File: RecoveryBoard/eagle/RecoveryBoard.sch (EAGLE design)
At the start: 96 parts, among them Q1 BSS123, Q2 BSS123, Q3 BSS123, Q4 BPR-301, Q5 BPR-301, Q6 MOSFET-PCH-SOT23-6, U1 STM32F042K6, U10 TPS63070, U2 BD62120AEFJ-E2, U3 H11F1SR2M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

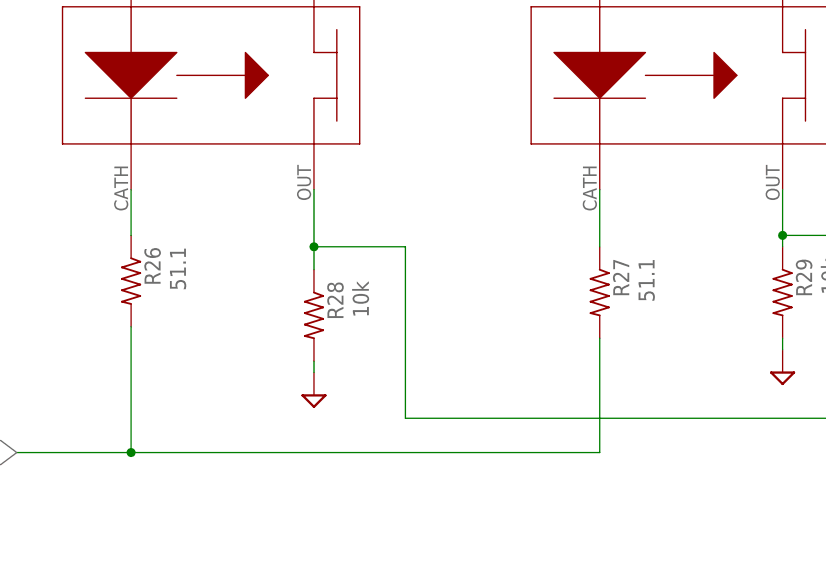
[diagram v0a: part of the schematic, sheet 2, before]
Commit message: added camera board folder and git ignore
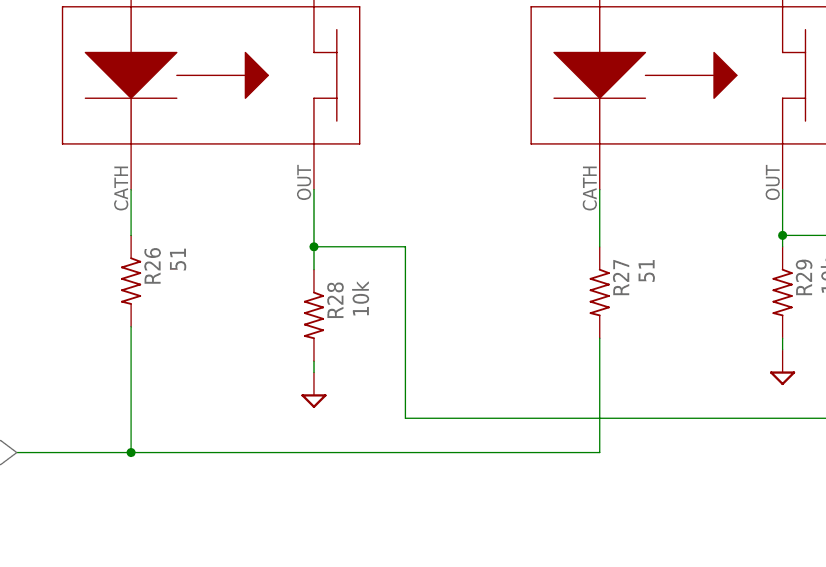
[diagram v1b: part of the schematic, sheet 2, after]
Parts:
- R26, R27: value 51.1 -> 51
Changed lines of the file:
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@@
 <part name="SUPPLY23" library="supply2" library_urn="urn:adsk.eagle:library:372" deviceset="GND" device=""/>
 <part name="SUPPLY5" library="SparkFun-PowerSymbols" library_urn="urn:adsk.eagle:library:530" deviceset="3.3V" device=""/>
-<part name="R26" library="oresat-rcl" deviceset="R-US_" device="0603-C-NOSILK" value="51.1"/>
-<part name="R27" library="oresat-rcl" deviceset="R-US_" device="0603-C-NOSILK" value="51.1"/>
+<part name="R26" library="oresat-rcl" deviceset="R-US_" device="0603-C-NOSILK" value="51"/>
+<part name="R27" library="oresat-rcl" deviceset="R-US_" device="0603-C-NOSILK" value="51"/>
 <part name="R28" library="oresat-rcl" deviceset="R-US_" device="0603-C-NOSILK" value="10k"/>
 <part name="R29" library="oresat-rcl" deviceset="R-US_" device="0603-C-NOSILK" value="10k"/>

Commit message: file names
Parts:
- R8, R9: value 442 -> 470
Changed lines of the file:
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@@
 <part name="SUPPLY4" library="supply2" library_urn="urn:adsk.eagle:library:372" deviceset="GND" device=""/>
 <part name="R7" library="oresat-rcl" deviceset="R-US_" device="0603-C-NOSILK" value="10k"/>
-<part name="R8" library="oresat-rcl" deviceset="R-US_" device="0603-C-NOSILK" value="442"/>
-<part name="R9" library="oresat-rcl" deviceset="R-US_" device="0603-C-NOSILK" value="442"/>
+<part name="R8" library="oresat-rcl" deviceset="R-US_" device="0603-C-NOSILK" value="470"/>
+<part name="R9" library="oresat-rcl" deviceset="R-US_" device="0603-C-NOSILK" value="470"/>
 <part name="R10" library="oresat-rcl" deviceset="R-US_" device="0603-C-NOSILK" value="10k"/>
 <part name="SUPPLY24" library="supply2" library_urn="urn:adsk.eagle:library:372" deviceset="GND" device=""/>
